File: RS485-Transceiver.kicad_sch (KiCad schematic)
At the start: 5 parts, among them IC1 THVD2410VDRCR, U12 DF52-4S-0.8H(21)

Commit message: fix vbat
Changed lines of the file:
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@@
+    (stroke (width 0) (type default))
+  )
+  (wire (pts (xy 55.88 104.14) (xy 52.07 104.14))
     (stroke (width 0) (type default))
   )
@@
     (stroke (width 0) (type default))
   )
-  (wire (pts (xy 55.245 84.455) (xy 52.705 84.455))
+  (wire (pts (xy 55.245 84.455) (xy 52.07 84.455))
     (stroke (width 0) (type default))
   )
@@
     (stroke (width 0) (type default))
   )
-  (wire (pts (xy 56.515 88.9) (xy 52.705 88.9))
+  (wire (pts (xy 56.515 88.9) (xy 52.07 88.9))
     (stroke (width 0) (type default))
   )
@@
     (stroke (width 0) (type default))
   )
-  (wire (pts (xy 56.515 97.79) (xy 52.705 97.79))
+  (wire (pts (xy 56.515 97.79) (xy 52.07 97.79))
     (stroke (width 0) (type default))
   )
-  (wire (pts (xy 55.88 80.01) (xy 52.705 80.01))
+  (wire (pts (xy 55.88 80.01) (xy 52.07 80.01))
     (stroke (width 0) (type default))
   )
@@
     (stroke (width 0) (type default))
   )
-  (wire (pts (xy 56.515 93.345) (xy 52.705 93.345))
+  (wire (pts (xy 56.515 93.345) (xy 52.07 93.345))
     (stroke (width 0) (type default))
   )
@@
     (effects (font (size 1.27 1.27)) (justify left bottom))
   )
+  (label "VBAT" (at 55.88 104.14 0) (fields_autoplaced)
+    (effects (font (size 1.27 1.27)) (justify left bottom))
+  )
   (label "UART_DE" (at 56.515 97.79 0) (fields_autoplaced)
     (effects (font (size 1.27 1.27)) (justify left bottom))
@@
     (effects (font (size 1.27 1.27)) (justify left bottom))
   )
-  (hierarchical_label "UART_TX" (shape input) (at 52.705 93.345 180) (fields_autoplaced)
+  (hierarchical_label "UART_TX" (shape input) (at 52.07 93.345 180) (fields_autoplaced)
     (effects (font (size 1.27 1.27)) (justify right))
   )
-  (hierarchical_label "DE" (shape input) (at 52.705 97.79 180) (fields_autoplaced)
+  (hierarchical_label "DE" (shape input) (at 52.07 97.79 180) (fields_autoplaced)
     (effects (font (size 1.27 1.27)) (justify right))
   )
@@
     (effects (font (size 1.27 1.27)) (justify right))
   )
-  (hierarchical_label "3V3" (shape input) (at 52.705 80.01 180) (fields_autoplaced)
+  (hierarchical_label "3V3" (shape input) (at 52.07 80.01 180) (fields_autoplaced)
     (effects (font (size 1.27 1.27)) (justify right))
   )
-  (hierarchical_label "UART_RX" (shape input) (at 52.705 88.9 180) (fields_autoplaced)
+  (hierarchical_label "UART_RX" (shape input) (at 52.07 88.9 180) (fields_autoplaced)
     (effects (font (size 1.27 1.27)) (justify right))
   )
-  (hierarchical_label "GND" (shape input) (at 52.705 84.455 180) (fields_autoplaced)
+  (hierarchical_label "GND" (shape input) (at 52.07 84.455 180) (fields_autoplaced)
     (effects (font (size 1.27 1.27)) (justify right))
   )
+  (hierarchical_label "VBAT" (shape input) (at 52.07 104.14 180) (fields_autoplaced)
+    (effects (font (size 1.27 1.27)) (justify right))
+  )

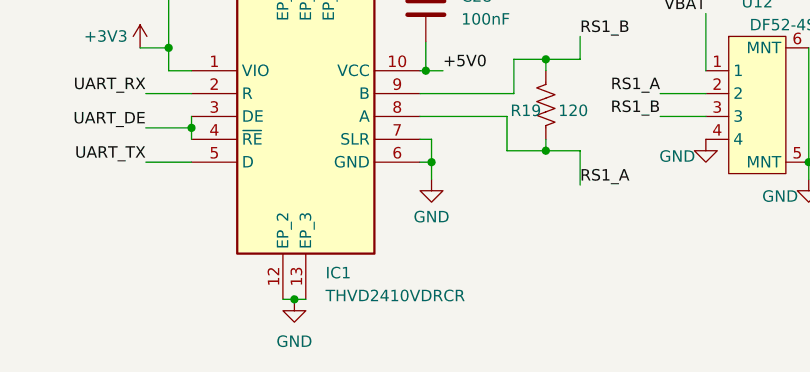
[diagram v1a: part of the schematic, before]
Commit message: bom fix for fets, now refers to the part i am actually using not the one which doesn't work right. Library changes for parts missing courtyards, drc passing
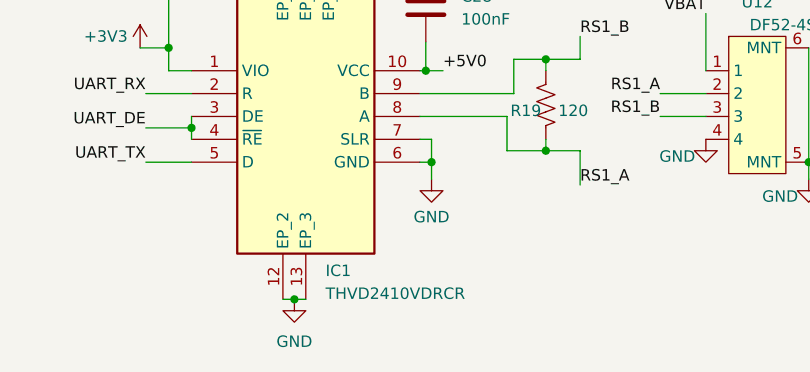
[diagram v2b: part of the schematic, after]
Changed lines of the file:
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@@
   (symbol (lib_id "SamacSys_Parts:THVD2410VDRCR") (at 103.505 89.535 0) (unit 1)
     (in_bom yes) (on_board yes) (dnp no) (fields_autoplaced)
-    (property "Reference" "IC1" (at 118.3991 112.014 0)
+    (property "Reference" "IC1" (at 118.3991 111.76 0)
       (effects (font (size 1.27 1.27)) (justify left))
     )
-    (property "Value" "THVD2410VDRCR" (at 118.3991 114.554 0)
+    (property "Value" "THVD2410VDRCR" (at 118.3991 114.3 0)
       (effects (font (size 1.27 1.27)) (justify left))
     )

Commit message: found better part
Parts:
- IC1: value THVD2410VDRCR -> THVD2450VDRCR; symbol SamacSys_Parts:THVD2410VDRCR -> robot-cortex:THVD2450VDRCR; Manufacturer_Part_Number THVD2410VDRCR -> THVD2450VDRCR
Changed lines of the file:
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@@
     (effects (font (size 1.27 1.27)) (justify right))
   )
-  (symbol (lib_id "SamacSys_Parts:THVD2410VDRCR") (at 103.505 89.535 0) (unit 1)
+  (symbol (lib_id "robot-cortex:THVD2450VDRCR") (at 103.505 89.535 0) (unit 1)
     (in_bom yes) (on_board yes) (dnp no) (fields_autoplaced)
     (property "Reference" "IC1" (at 118.3991 111.76 0)
       (effects (font (size 1.27 1.27)) (justify left))
     )
-    (property "Value" "THVD2410VDRCR" (at 118.3991 114.3 0)
+    (property "Value" "THVD2450VDRCR" (at 118.3991 114.3 0)
       (effects (font (size 1.27 1.27)) (justify left))
     )
@@
       (effects (font (size 1.27 1.27)) (justify left top) hide)
     )
-    (property "Manufacturer_Part_Number" "THVD2410VDRCR" (at 125.095 676.835 0)
+    (property "Manufacturer_Part_Number" "THVD2450VDRCR" (at 125.095 676.835 0)
       (effects (font (size 1.27 1.27)) (justify left top) hide)
     )
